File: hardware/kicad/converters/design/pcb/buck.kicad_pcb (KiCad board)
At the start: 2 copper layers, 120 x 56 mm, 11 parts, among them J1 V1 ind (15V), J2 5V ud, J3 PWM (isoleret), J4 gate-forsyning, M1 IRF530N, U1 4N25

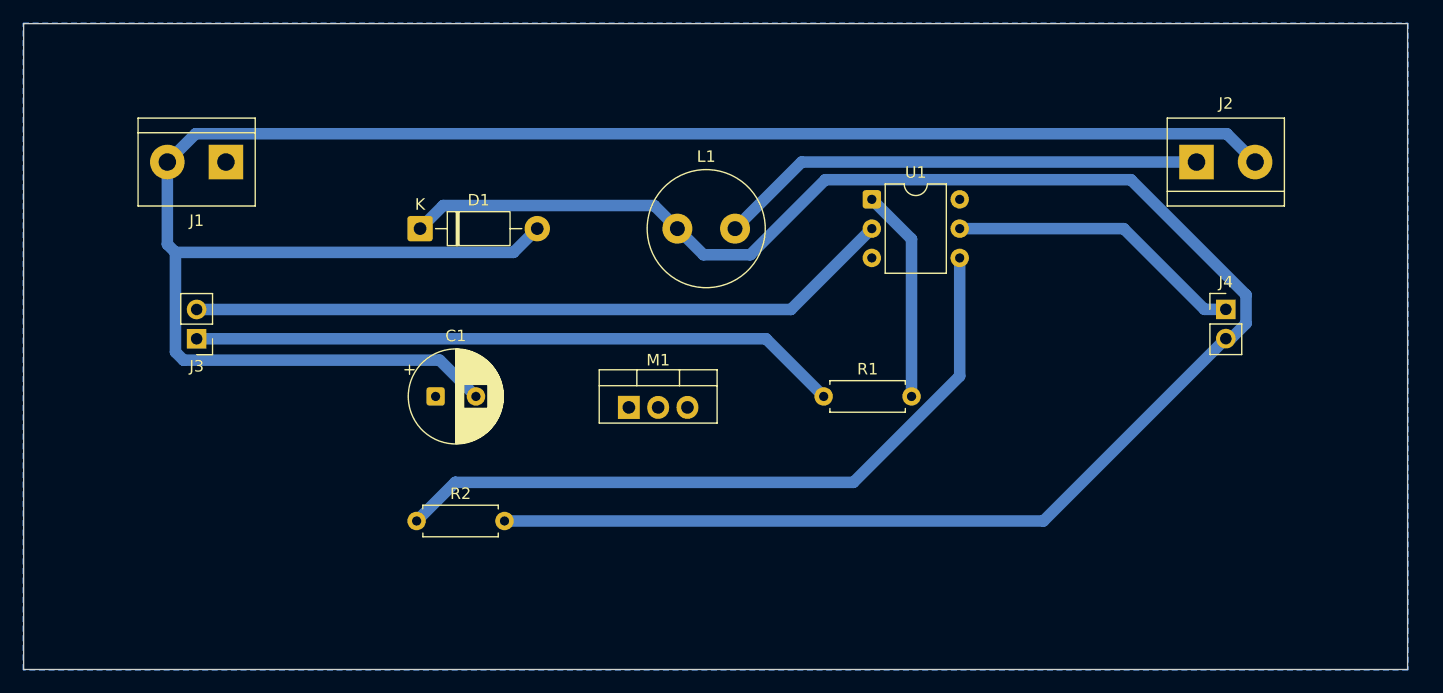
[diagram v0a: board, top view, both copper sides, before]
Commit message: Apply fiber-laser design rules from the DTU-PCB-prototyping guide
All seven boards rebuilt to meet the XTool fiber laser workflow
(SimsesLab/DTU-PCB-prototyping): 1.0 mm tracks, 0.8 mm clearance, solid
no-net fill zone on B.Cu (pad connection: none) so the laser only
engraves the isolation channels, DIP footprints switched to the
_LongPads variants from the guide's shop table.

TO packages cannot meet 0.8 mm pad-to-pad at stock sizes, so
energy_system.pretty now has TO-220-3_Vertical_LaserPads (pads narrowed
to 1.7 mm -> 0.84 mm gap; make_laserpads.py regenerates). The MPPT pass
transistor moves BD139 -> TIP41A (shop part): TO-126's 2.28 mm pitch can
never satisfy the rule, and TO-220 handles the ~7 W better anyway.

Two more bugs caught in this pass:
- Device:Q_NMOS uses letter pin numbers (G/D/S) while TO-220 pads are
  1/2/3 - buck/boost MOSFET pads silently got NO net in the earlier
  boards (no-net pads don't count as unconnected). pcb_build.py now maps
  G/D/S->1/2/3 and fails hard if a component ends up netless.
- DRC now 0 violations on all seven boards; remaining airwires are the
  documented jumpers.
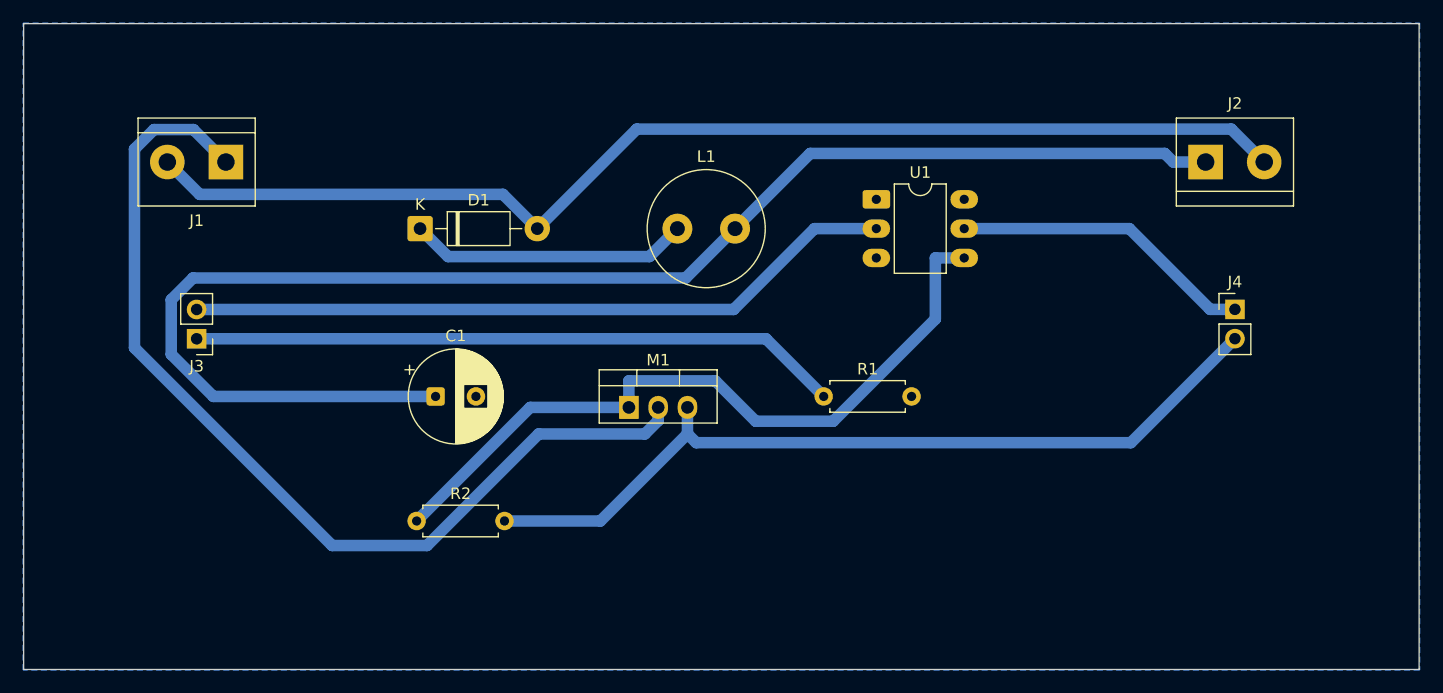
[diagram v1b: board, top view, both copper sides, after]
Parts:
- M1: footprint TO-220-3_Vertical -> TO-220-3_Vertical_LaserPads
- U1: footprint DIP-6_W7.62mm -> DIP-6_W7.62mm_LongPads
- moved J4 0.79 mm to (125.0, 44.8)
- moved J2 0.79 mm to (122.5, 32.0)
- moved U1 0.39 mm to (93.9, 35.2)
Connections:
- M1 pad 1: (no net) -> GATE
- M1 pad 2: (no net) -> /VIN_15V
- M1 pad 3: (no net) -> /SW
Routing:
- net /VIN_15V: track 0.00 -> 85.2 mm
- net /VOUT_5V: track 42.4 -> 124.4 mm
- net /GND: track 173.0 -> 102.3 mm
- net /SW: track 154.9 -> 97.1 mm
- net Net-(R1-Pad2): track 18.5 -> 0.00 mm
- net GATE: track 62.5 -> 64.3 mm
- added copper zone on B.Cu, net (none)
- removed copper zone on B.Cu, net /GND
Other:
- board size 120 x 56 mm -> 121 x 56 mm

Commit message: Engrave component references into the copper on all boards
The fiber laser has no silkscreen step, so the refdes (R1, U1, ...) are
placed as mirrored copper text on B.Cu next to each component - they
engrave in the same run as the traces and read correctly from the
solder side. Placement is collision-checked against tracks/pads/other
text (copper text over a track would short or sever it); tracks are
sampled into small boxes so diagonal runs don't false-positive. 86 of
96 labels fit; the handful dropped in dense spots are listed in
production/README.md and still appear on the F_Fab plots.

Also exports <board>_silk_top.dxf (F.Silkscreen + outline) per board as
an optional top-side engraving pass - run it on the component side
BEFORE the copper run, and do NOT mirror that one.

DRC still 0 violations on all seven; jumper lists updated.
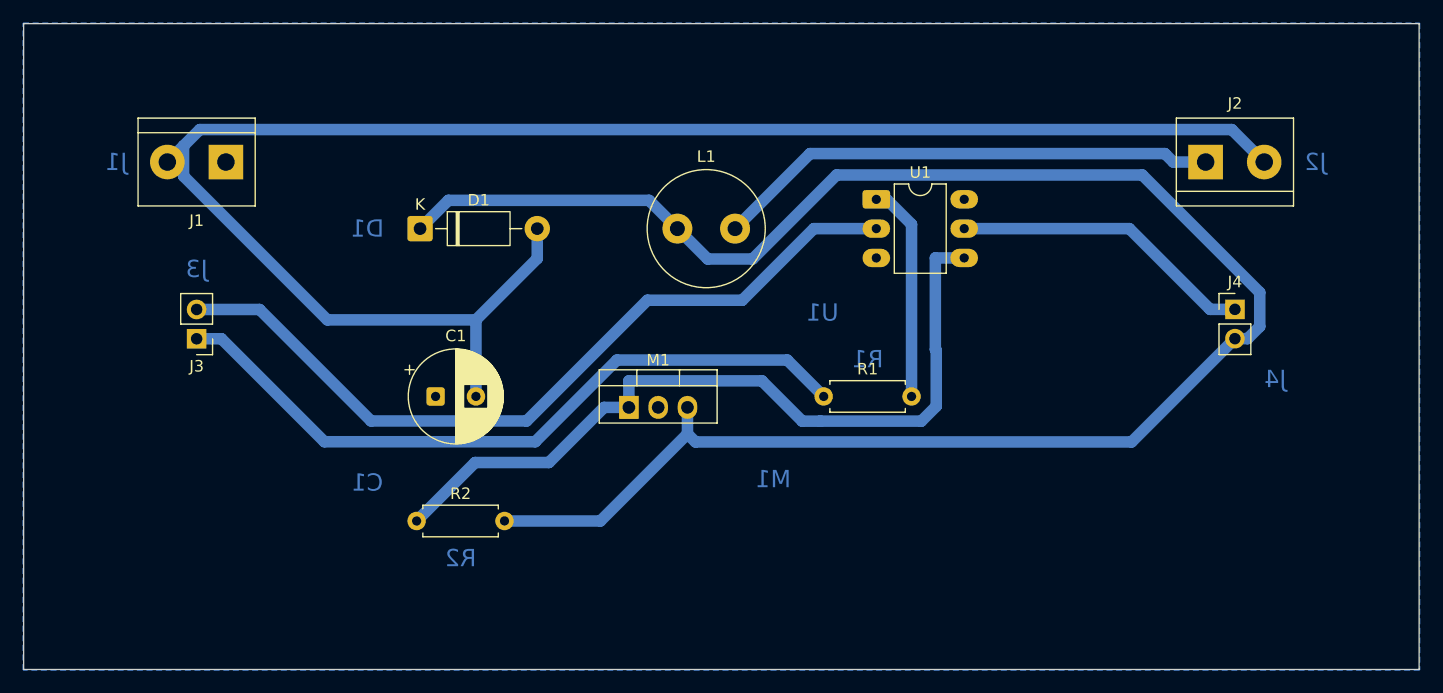
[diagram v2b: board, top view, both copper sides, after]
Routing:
- net /VIN_15V: track 85.2 -> 0.00 mm
- net /VOUT_5V: track 124.4 -> 43.8 mm
- net /SW: track 97.1 -> 161.5 mm
- net /GND: track 102.3 -> 147.3 mm
- net Net-(R1-Pad2): track 0.00 -> 18.9 mm
- net GND_MCU: track 61.8 -> 69.8 mm
- net PWM: track 56.4 -> 62.3 mm
- net GATE: track 64.3 -> 68.8 mm
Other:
- board text added: "C1"
- board text added: "D1"
- board text added: "J1"
- board text added: "J2"
- board text added: "J3"
- board text added: "J4"
- board text added: "M1"
- board text added: "R1"
- board text added: "R2"
- board text added: "U1"
